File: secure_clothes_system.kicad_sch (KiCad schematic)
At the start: 6 parts, among them U1 TPS62842DGRR

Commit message: Made some fixes with the layout
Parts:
- C1: footprint Capacitor_SMD:C_0603_1608Metric -> Capacitor_SMD:C_0402_1005Metric; Descrip CAP CER 4.7UF 10V X7R 0603 -> CAP CER 4.7UF 10V X5R 0402; Manufacturer Murata Electronics -> Samsung Electro-Mechanics; Mfg Part # GRM188Z71A475KE15D -> CL05A475MP5NRNC; Price 0,05871 -> 0,01360; TC X7R -> X5R; Tol ±10% -> ±20%
- C2: footprint Capacitor_SMD:C_0805_2012Metric -> Capacitor_SMD:C_0402_1005Metric; Descrip CAP CER 10UF 10V X5R 0805 -> CAP CER 10UF 6.3V X5R 0402; Manufacturer Samsung Electro-Mechanics -> Murata Electronics; Mfg Part # CL21A106KPFNNNE -> GRM155R60J106ME15D; Price 0,02060 -> 0,02240; VOLTAGE 10V -> 6.3V
- R1: value 267K -> 52.3K; footprint Resistor_SMD:R_0603_1608Metric -> Resistor_SMD:R_0402_1005Metric; Descrip RES 267K OHM 1% 1/10W 0603 -> RES 52.3K OHM 1% 1/16W 0402; Mfg Part # RC0603FR-07267KL -> RC0402FR-0752K3L; Power (none) -> 0.063W, 1/16W; Price 0,00510 -> 0,00306; Tol (none) -> ±1%
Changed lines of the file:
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@@
 		(fields_autoplaced yes)
 		(property "Reference" "R1"
-			(at 127 109.22 0)
+			(at 127 109.2199 0)
 			(effects
 				(font
@@
 			)
 		)
-		(property "Value" "267K"
-			(at 127 111.76 0)
+		(property "Value" "52.3K"
+			(at 127 111.7599 0)
 			(effects
 				(font
@@
 			)
 		)
-		(property "Footprint" "Resistor_SMD:R_0603_1608Metric"
+		(property "Footprint" "Resistor_SMD:R_0402_1005Metric"
 			(at 125.476 110.744 90)
 			(effects
@@
 			)
 		)
-		(property "Price" "0,00510"
+		(property "Price" "0,00306"
 			(at 124.46 110.49 0)
 			(effects
@@
 			)
 		)
-		(property "Mfg Part #" "RC0603FR-07267KL"
+		(property "Mfg Part #" "RC0402FR-0752K3L"
 			(at 124.46 110.49 0)
 			(effects
@@
 			)
 		)
-		(property "Descrip" "RES 267K OHM 1% 1/10W 0603"
+		(property "Descrip" "RES 52.3K OHM 1% 1/16W 0402"
 			(at 124.46 110.49 0)
 			(effects
@@
 			)
 		)
-		(property "Power" ""
-			(at 124.46 110.49 0)
-			(effects
-				(font
-					(size 1.27 1.27)
-				)
-			)
-		)
-		(property "Tol" ""
-			(at 124.46 110.49 0)
-			(effects
-				(font
-					(size 1.27 1.27)
-				)
+		(property "Power" "0.063W, 1/16W"
+			(at 124.46 110.49 0)
+			(effects
+				(font
+					(size 1.27 1.27)
+				)
+				(hide yes)
+			)
+		)
+		(property "Tol" "±1%"
+			(at 124.46 110.49 0)
+			(effects
+				(font
+					(size 1.27 1.27)
+				)
+				(hide yes)
 			)
 		)
@@
 		(lib_id "Device:C")
 		(at 80.01 96.52 0)
-		(mirror y)
 		(unit 1)
 		(exclude_from_sim no)
@@
 		(on_board yes)
 		(dnp no)
-		(fields_autoplaced yes)
 		(property "Reference" "C1"
+			(at 76.2 92.7099 0)
+			(effects
+				(font
+					(size 1.27 1.27)
+				)
+				(justify right)
+			)
+		)
+		(property "Value" "4.7uF"
 			(at 76.2 95.2499 0)
 			(effects
@@
 					(size 1.27 1.27)
 				)
-				(justify left)
-			)
-		)
-		(property "Value" "4.7uF"
-			(at 76.2 97.7899 0)
-			(effects
-				(font
-					(size 1.27 1.27)
-				)
-				(justify left)
-			)
-		)
-		(property "Footprint" "Capacitor_SMD:C_0603_1608Metric"
-			(at 79.0448 100.33 0)
-			(effects
-				(font
-					(size 1.27 1.27)
-				)
-				(hide yes)
-			)
-		)
-		(property "Datasheet" "https://search.murata.co.jp/Ceramy/image/img/A01X/G101/ENG/GRM188Z71A475KE15-01.pdf"
+				(justify right)
+			)
+		)
+		(property "Footprint" "Capacitor_SMD:C_0402_1005Metric"
+			(at 80.9752 100.33 0)
+			(effects
+				(font
+					(size 1.27 1.27)
+				)
+				(hide yes)
+			)
+		)
+		(property "Datasheet" "https://mm.digikey.com/Volume0/opasdata/d220001/medias/docus/863/CL05A475MP5NRNC_Spec.pdf"
 			(at 80.01 96.52 0)
 			(effects
@@
 			)
 		)
-		(property "Manufacturer" "Murata Electronics"
+		(property "Manufacturer" "Samsung Electro-Mechanics"
 			(at 80.01 96.52 0)
 			(effects
@@
 			)
 		)
-		(property "Price" "0,05871"
+		(property "Price" "0,01360"
 			(at 80.01 96.52 0)
 			(effects
@@
 			)
 		)
-		(property "Mfg Part #" "GRM188Z71A475KE15D"
+		(property "Mfg Part #" "CL05A475MP5NRNC"
 			(at 80.01 96.52 0)
 			(effects
@@
 			)
 		)
-		(property "Descrip" "CAP CER 4.7UF 10V X7R 0603"
+		(property "Descrip" "CAP CER 4.7UF 10V X5R 0402"
 			(at 80.01 96.52 0)
 			(effects
@@
 			)
 		)
-		(property "TC" "X7R"
-			(at 80.01 96.52 0)
-			(effects
-				(font
-					(size 1.27 1.27)
-				)
-				(hide yes)
+		(property "TC" "X5R"
+			(at 76.2 97.7899 0)
+			(effects
+				(font
+					(size 1.27 1.27)
+				)
+				(justify right)
 			)
 		)
@@
 		)
 		(property "VOLTAGE" "10V"
-			(at 76.2 99.0599 0)
-			(effects
-				(font
-					(size 1.27 1.27)
-				)
-				(justify left)
-				(hide yes)
+			(at 76.2 100.3299 0)
+			(effects
+				(font
+					(size 1.27 1.27)
+				)
+				(justify right)
 			)
 		)
@@
 			)
 		)
-		(property "Tol" "±10%"
+		(property "Tol" "±20%"
 			(at 80.01 96.52 0)
 			(effects
@@
 		(fields_autoplaced yes)
 		(property "Reference" "C2"
-			(at 142.24 96.5199 0)
+			(at 142.24 95.2499 0)
 			(effects
 				(font
@@
 		)
 		(property "Value" "10uF"
-			(at 142.24 99.0599 0)
+			(at 142.24 97.7899 0)
 			(effects
 				(font
@@
 			)
 		)
-		(property "Footprint" "Capacitor_SMD:C_0805_2012Metric"
+		(property "Footprint" "Capacitor_SMD:C_0402_1005Metric"
 			(at 139.3952 102.87 0)
 			(effects
@@
 			)
 		)
-		(property "Datasheet" "https://mm.digikey.com/Volume0/opasdata/d220001/medias/docus/926/CL_Series_MLCC_ds.pdf"
+		(property "Datasheet" "https://www.murata.com/en-us/api/pdfdownloadapi?cate=luCeramicCapacitorsSMD&partno=GRM155R60J106ME15%23"
 			(at 138.43 99.06 0)
 			(effects
@@
 			)
 		)
-		(property "Manufacturer" "Samsung Electro-Mechanics"
+		(property "Manufacturer" "Murata Electronics"
 			(at 138.43 99.06 0)
 			(effects
@@
 			)
 		)
-		(property "Price" "0,02060"
+		(property "Price" "0,02240"
 			(at 138.43 99.06 0)
 			(effects
@@
 		)
 		(property "TC" "X5R"
-			(at 142.24 101.5999 0)
+			(at 142.24 100.3299 0)
 			(effects
 				(font
@@
 			)
 		)
-		(property "Mfg Part #" "CL21A106KPFNNNE"
+		(property "Mfg Part #" "GRM155R60J106ME15D"
 			(at 138.43 99.06 0)
 			(effects
@@
 			)
 		)
-		(property "VOLTAGE" "10V"
-			(at 138.43 99.06 0)
-			(effects
-				(font
-					(size 1.27 1.27)
-				)
-				(hide yes)
+		(property "VOLTAGE" "6.3V"
+			(at 142.24 102.8699 0)
+			(effects
+				(font
+					(size 1.27 1.27)
+				)
+				(justify left)
 			)
 		)
@@
 			)
 		)
-		(property "Descrip" "CAP CER 10UF 10V X5R 0805"
+		(property "Descrip" "CAP CER 10UF 6.3V X5R 0402"
 			(at 138.43 99.06 0)
 			(effects

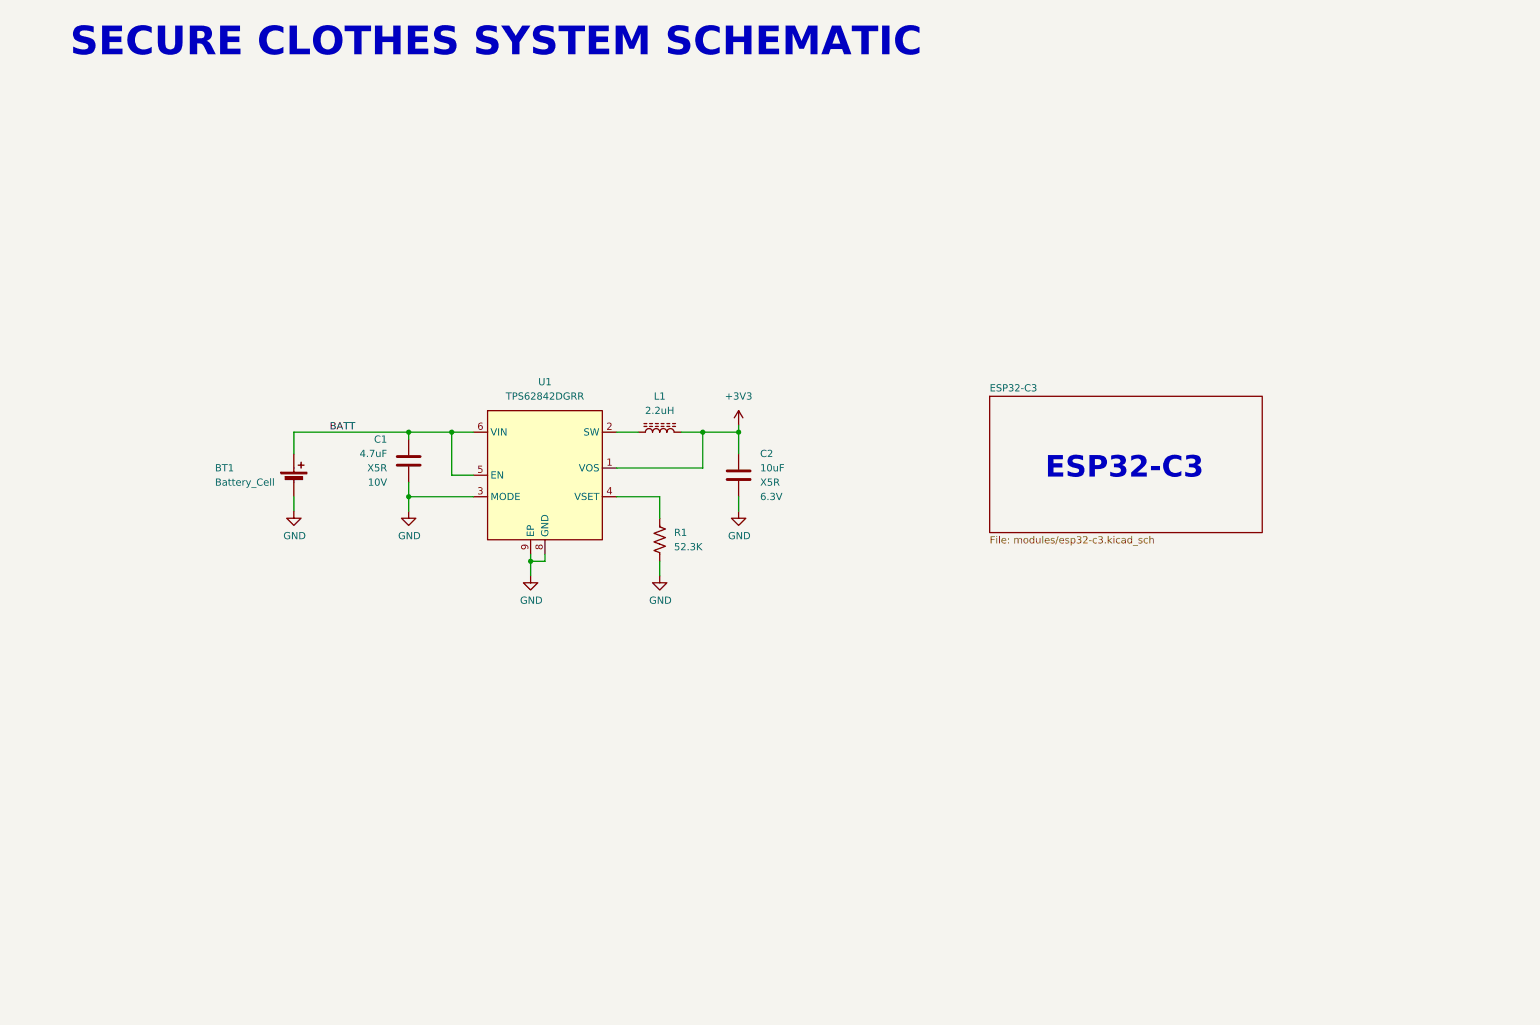
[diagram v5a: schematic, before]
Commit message: Solved some warnings
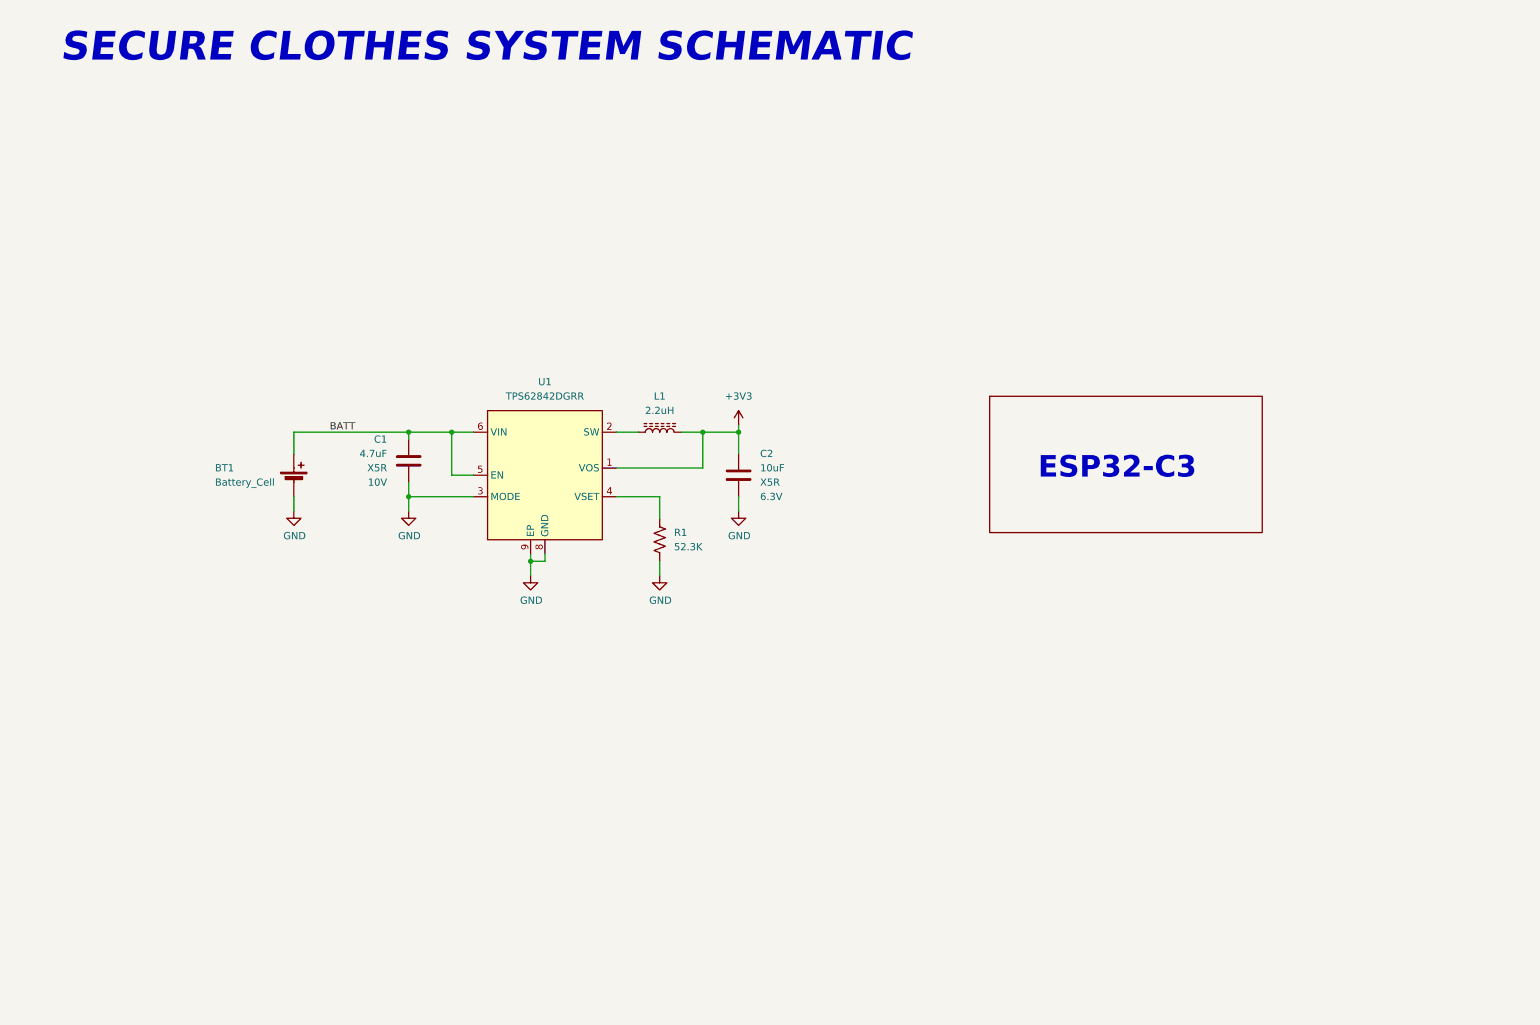
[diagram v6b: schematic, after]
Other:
- title: (none) -> ${TITLE}
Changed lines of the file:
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@@
 	(paper "A4")
 	(title_block
+		(title "${TITLE}")
 		(date "2024-12-11")
 		(rev "${VERSION}")
@@
 	(text "SECURE CLOTHES SYSTEM SCHEMATIC"
 		(exclude_from_sim no)
-		(at 20.066 25.4 0)
+		(at 93.726 23.368 0)
 		(effects
 			(font
@@
 				(thickness 1.016)
 				(bold yes)
-			)
-			(justify left bottom)
+				(italic yes)
+			)
 		)
 	)
 	(text "ESP32-C3"
 		(exclude_from_sim no)
-		(at 206.756 97.79 0)
+		(at 205.486 97.79 0)
 		(effects
 			(font
@@
 		)
 		(fill
-			(color 0 0 0 0.0000)
+			(color 178 242 187 1.0000)
 		)
 		(property "Sheetname" "ESP32-C3"
@@
 				)
 				(justify left bottom)
+				(hide yes)
 			)
 		)
@@
 				)
 				(justify left top)
-			)
-		)
+				(hide yes)
+			)
+		)

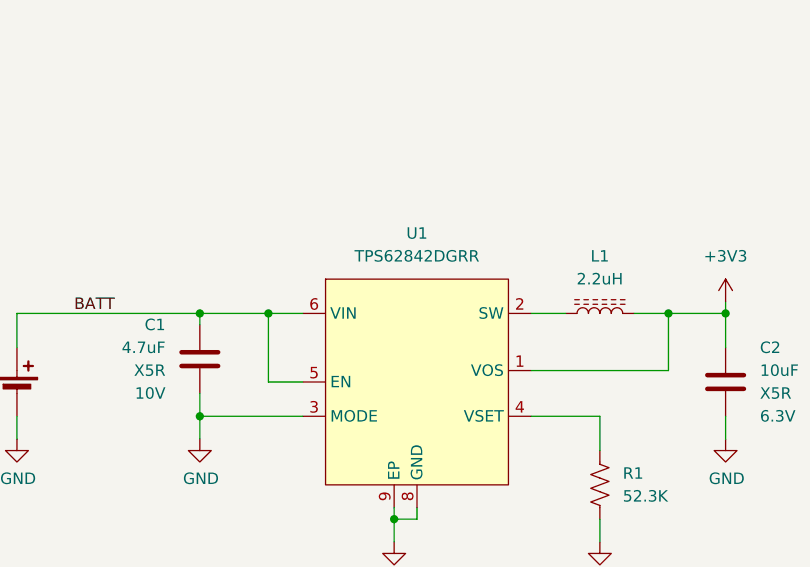
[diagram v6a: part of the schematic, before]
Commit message: Fabrication.kicad_jobset added.
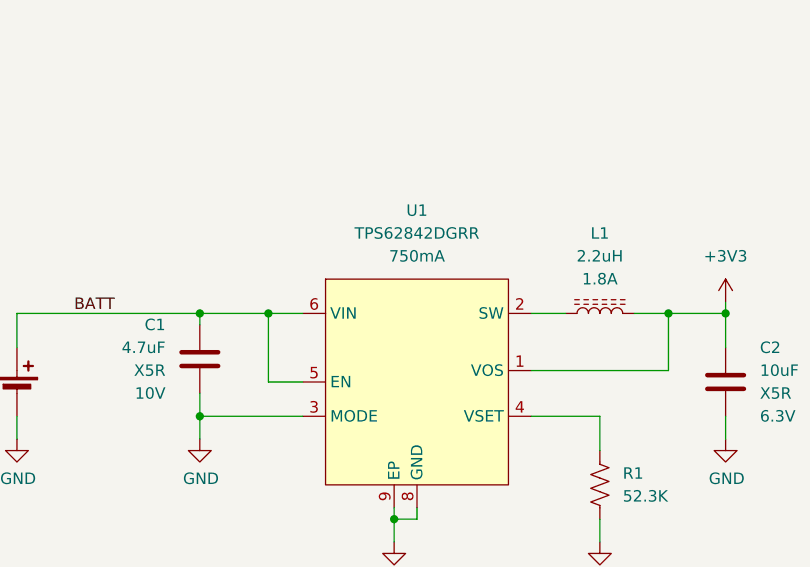
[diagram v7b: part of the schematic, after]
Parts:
- C1: Cost (none) -> 0,01360; Descrip CAP CER 4.7UF 10V X5R 0402 -> (none); PROVIDER Digikey -> (none); Price 0,01360 -> (none); Supplier (none) -> Digikey; VOLTAGE 10V -> (none); Voltage (none) -> 10V
- C2: Cost (none) -> 0,02240; Descrip CAP CER 10UF 6.3V X5R 0402 -> (none); PROVIDER Digikey -> (none); Price 0,02240 -> (none); Supplier (none) -> Digikey; VOLTAGE 6.3V -> (none); Voltage (none) -> 6.3V
- L1: CURRENT 1.8A -> (none); Cost (none) -> 0,14588; Current (none) -> 1.8A; Descrip FIXED IND 2.2UH 1.8A 116MOHM SMD -> (none); PROVIDER Digikey -> (none); Price 0,14588 -> (none); Supplier (none) -> Digikey
- R1: Cost (none) -> 0,00306; Descrip RES 52.3K OHM 1% 1/16W 0402 -> (none); PROVIDER Digikey -> (none); Price 0,00306 -> (none); Supplier (none) -> Digikey
- U1: CURRENT 750mA -> (none); Cost (none) -> 0,93834; Current (none) -> 750mA; Descrip IC REG BUCK ADJ 750MA 8HVSSOP -> (none); PROVIDER Digikey -> (none); Price 0,93834 -> (none); Supplier (none) -> Digikey
